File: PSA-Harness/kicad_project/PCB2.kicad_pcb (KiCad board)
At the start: 4 copper layers, 28.3 x 52.5 mm, 15 parts, among them J1 to_EPS_1, J2 to_EPS_2, J3 to_ESP_3, J7 USB_C_Receptacle, J8 B2B_1, J9 B2B_2, U1 DG419LEUA, U2 DG419LEUA

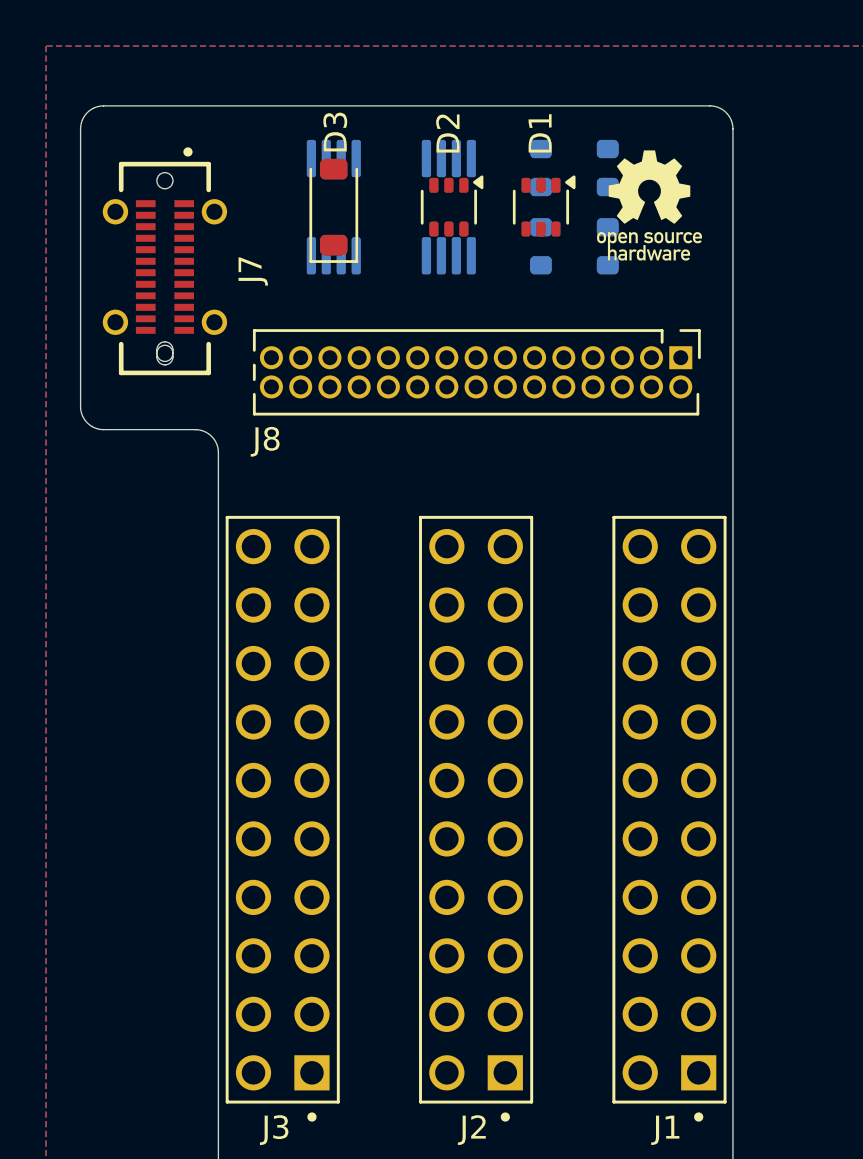
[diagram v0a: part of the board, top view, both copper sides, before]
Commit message: PCB2 CAN routed
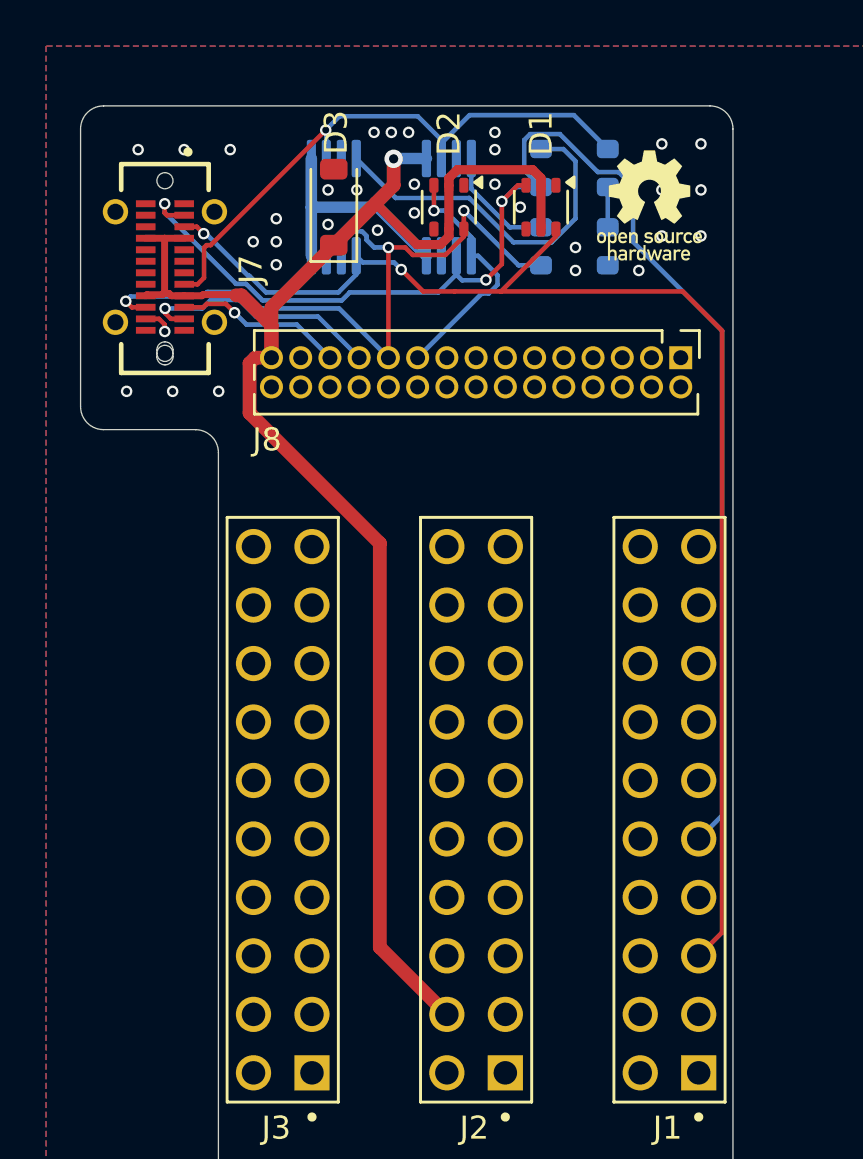
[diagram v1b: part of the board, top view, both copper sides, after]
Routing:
- net +12V: track 0.00 -> 79.9 mm, vias 0 -> 1
- net CAN0_H: track 0.00 -> 64.1 mm, vias 0 -> 3
- net CAN0_L: track 0.00 -> 58.3 mm, vias 0 -> 2
- net CAN2_L: track 0.00 -> 31.1 mm, vias 0 -> 3
- net SBU1: track 0.00 -> 26.5 mm, vias 0 -> 1
- net CAN2_H: track 0.00 -> 25.6 mm, vias 0 -> 2
- net Net-(R2-Pad1): track 0.00 -> 15.7 mm
- net CAN1_H: track 0.00 -> 10.8 mm, vias 0 -> 1
- net CAN1_L: track 0.00 -> 7.36 mm, vias 0 -> 1
- net Net-(R1-Pad2): track 0.00 -> 5.03 mm
- net Net-(R3-Pad2): track 0.00 -> 1.75 mm
- net GND: vias 0 -> 32

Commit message: PCB2 routed
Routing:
- net 1: track 0.00 -> 52.2 mm, vias 0 -> 3
- net 50: track 0.00 -> 50.3 mm, vias 0 -> 2
- net 49: track 0.00 -> 48.8 mm, vias 0 -> 3
- net 54: track 0.00 -> 45.4 mm, vias 0 -> 4
- net 48: track 0.00 -> 43.2 mm, vias 0 -> 1
- net 2: track 0.00 -> 41.3 mm, vias 0 -> 1
- net 28: track 0.00 -> 38.1 mm, vias 0 -> 1
- net 30: track 0.00 -> 38.0 mm, vias 0 -> 1
- net 52: track 0.00 -> 37.6 mm, vias 0 -> 2
- net 47: track 0.00 -> 37.6 mm, vias 0 -> 1
- net 4: track 0.00 -> 36.6 mm, vias 0 -> 3
- net 40: track 0.00 -> 35.7 mm
- net 60: track 0.00 -> 33.4 mm
- net 21: track 0.00 -> 33.3 mm, vias 0 -> 1
- net 29: track 0.00 -> 33.0 mm, vias 0 -> 1
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
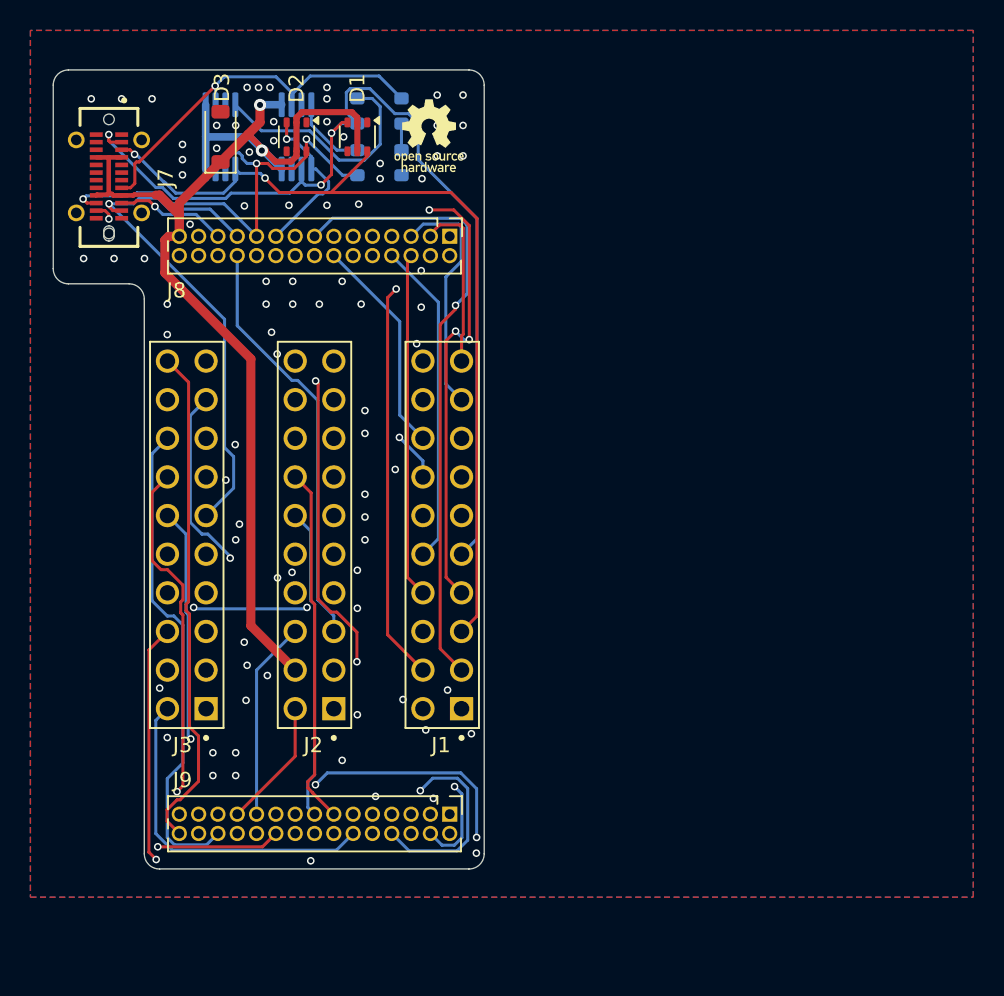
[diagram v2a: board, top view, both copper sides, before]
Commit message: improve PCB2 clearences
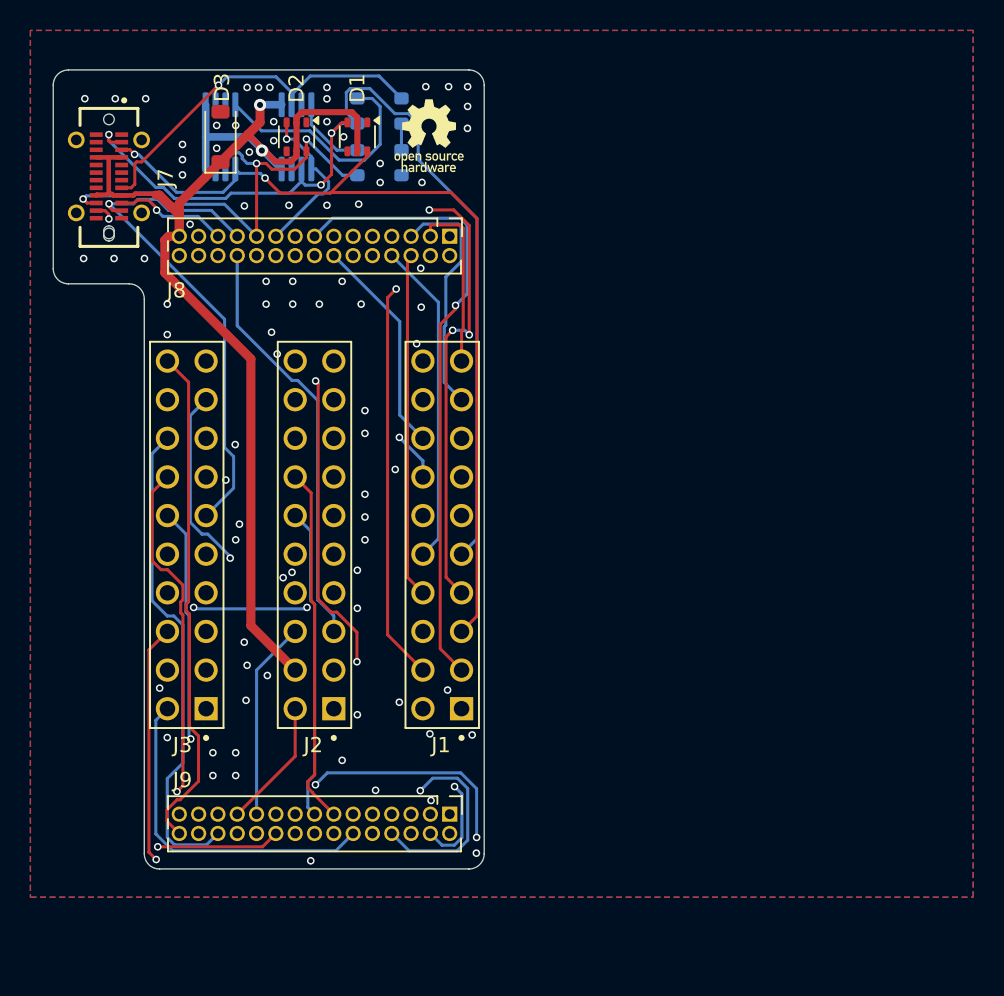
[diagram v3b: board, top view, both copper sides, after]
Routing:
- net GND: vias 68 -> 67
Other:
- rule pad_to_mask_clearance: 0.038 -> 0

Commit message: chg: separate PCB1/2
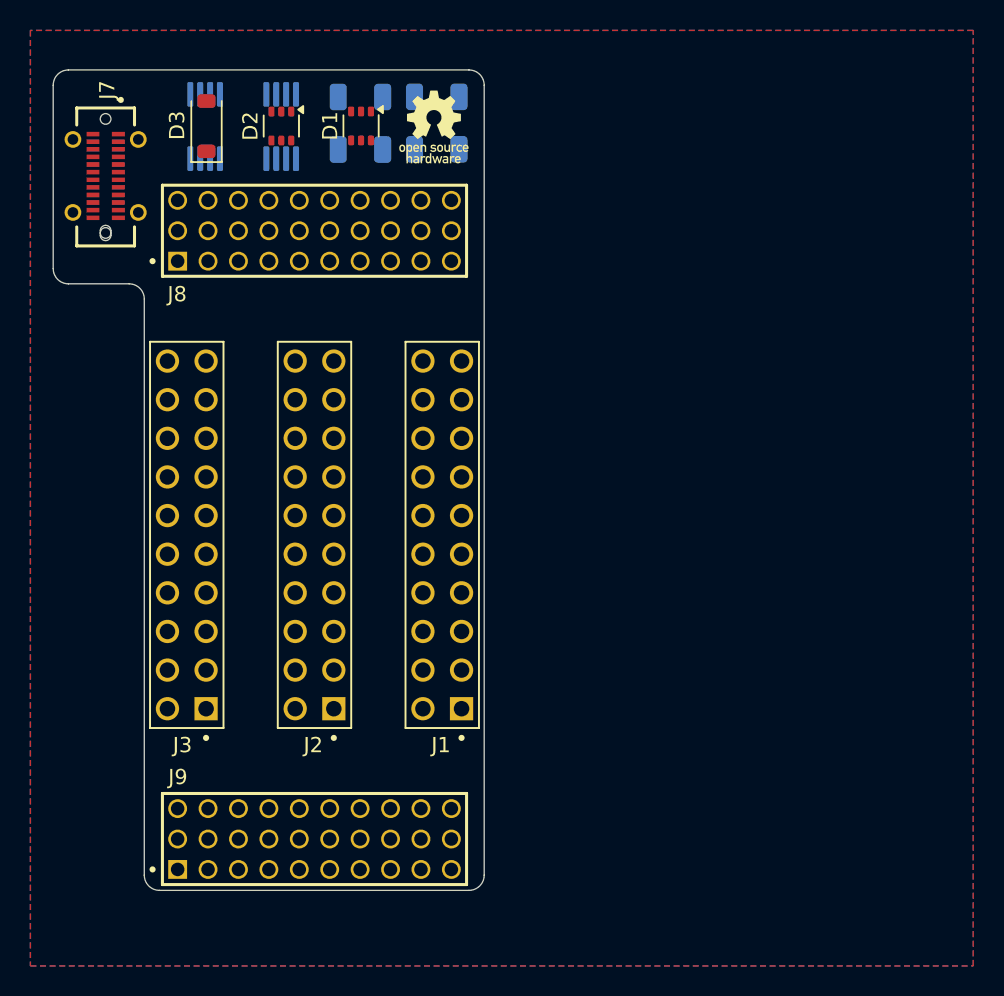
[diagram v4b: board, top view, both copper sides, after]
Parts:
- J8, J9: footprint Connector_PinHeader_1.27mm:PinHeader_2x15_P1.27mm_Vertical -> PSA:SAMTEC_TW-10-X-X-T-X-X
- R1, R2, R3, R4: footprint Resistor_SMD:R_0603_1608Metric -> Resistor_SMD:R_1206_3216Metric
- moved J9 18.3 mm to (96.7, 144.2), turned to 0 degrees
- moved J8 18.0 mm to (96.7, 104.2), turned to 0 degrees
- moved R3 2.50 mm to (113.7, 93.4), turned to 0 degrees
- moved R4 2.48 mm to (113.7, 96.8), turned to 180 degrees
- moved D2 1.23 mm to (103.5, 95.3)
- moved U1 1.22 mm to (98.5, 95.3)
- moved U2 1.22 mm to (103.5, 95.3)
- moved D3 1.16 mm to (98.6, 95.3)
- moved R2 0.94 mm to (108.7, 93.4), turned to 0 degrees
- moved R1 0.89 mm to (108.7, 96.8), turned to 180 degrees
- moved D1 0.76 mm to (108.7, 95.3)
- moved J7 0.22 mm to (91.9, 98.6)
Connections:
- J8 pad 1: 11 -> GND
- J8 pad 11: 6 -> CAN2_H
- J8 pad 13: 4 -> 1
- J8 pad 17: 1 -> 4
- J8 pad 19: CAN2_H -> 6
- J8 pad 21: CAN2_L -> 7
- J8 pad 23: CAN1_H -> 8
- J8 pad 25: CAN1_L -> 9
- J8 pad 27: GND -> 10
- J8 pad 29: +12V -> 11
- J8 pad 3: 10 -> +12V
- J8 pad 5: 9 -> CAN1_L
- J8 pad 7: 8 -> CAN1_H
- J8 pad 9: 7 -> CAN2_L
- J9 pad 1: 43 -> 28
- J9 pad 11: 38 -> 34
- J9 pad 13: 37 -> 35
- J9 pad 17: 35 -> 37
- J9 pad 19: 34 -> 38
- J9 pad 21: 33 -> 39
- J9 pad 23: 31 -> 40
- J9 pad 25: 30 -> 41
- J9 pad 27: 29 -> 42
- J9 pad 29: 28 -> 43
- J9 pad 3: 42 -> 29
- J9 pad 5: 41 -> 30
- J9 pad 7: 40 -> 31
- J9 pad 9: 39 -> 33
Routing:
- net +12V: track 80.2 -> 0.00 mm, vias 2 -> 0
- net CAN0_H: track 64.1 -> 0.00 mm, vias 3 -> 0
- net CAN0_L: track 58.3 -> 0.00 mm, vias 2 -> 0
- net 1: track 52.2 -> 0.00 mm, vias 3 -> 0
- net 50: track 50.3 -> 0.00 mm, vias 2 -> 0
- net 49: track 48.8 -> 0.00 mm, vias 3 -> 0
- net 54: track 45.4 -> 0.00 mm, vias 4 -> 0
- net 48: track 43.5 -> 0.00 mm, vias 1 -> 0
- net 2: track 41.3 -> 0.00 mm, vias 1 -> 0
- net 28: track 38.1 -> 0.00 mm, vias 1 -> 0
- net 30: track 38.0 -> 0.00 mm, vias 1 -> 0
- net 52: track 37.6 -> 0.00 mm, vias 2 -> 0
- net 47: track 37.6 -> 0.00 mm, vias 1 -> 0
- net 4: track 36.3 -> 0.00 mm, vias 3 -> 0
- net 40: track 35.7 -> 0.00 mm
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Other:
- board size 28.3 x 52.5 mm -> 28.3 x 54 mm
- rule pad_to_mask_clearance: 0 -> 0.038

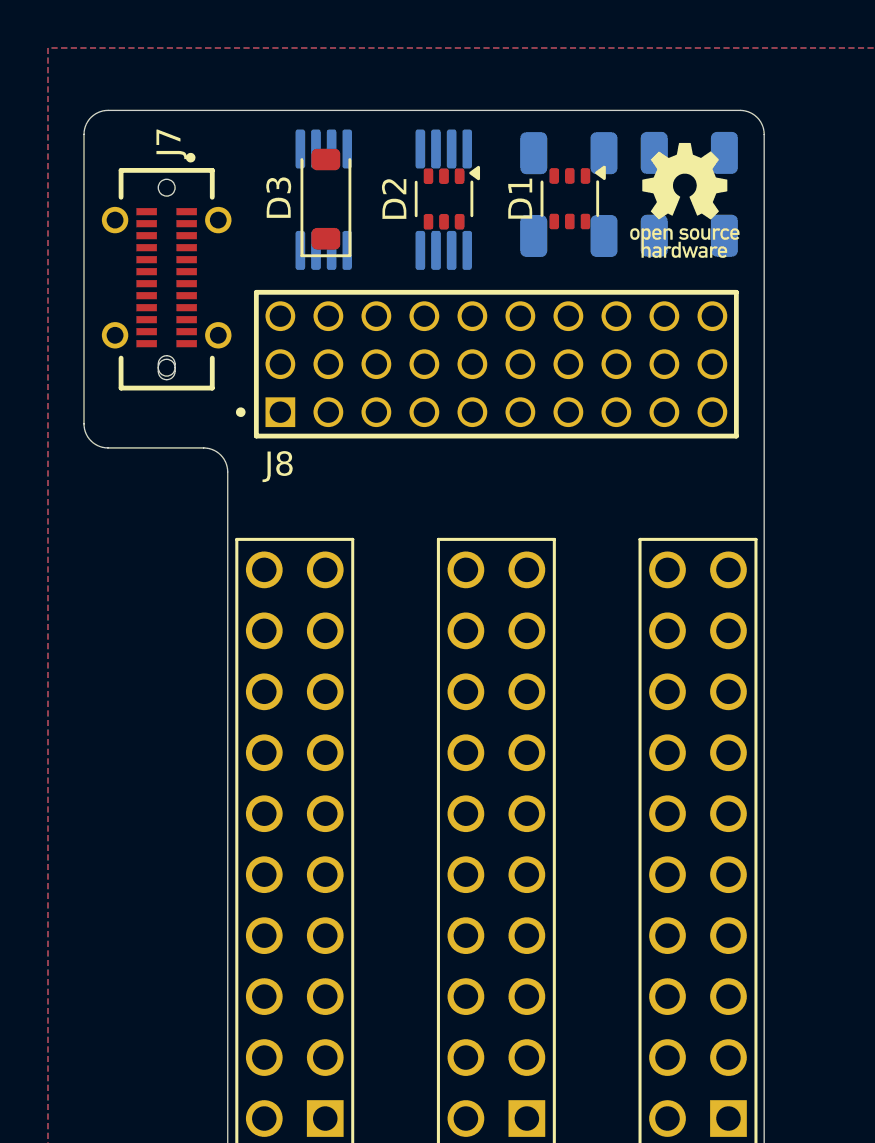
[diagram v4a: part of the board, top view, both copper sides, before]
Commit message: CAN routed
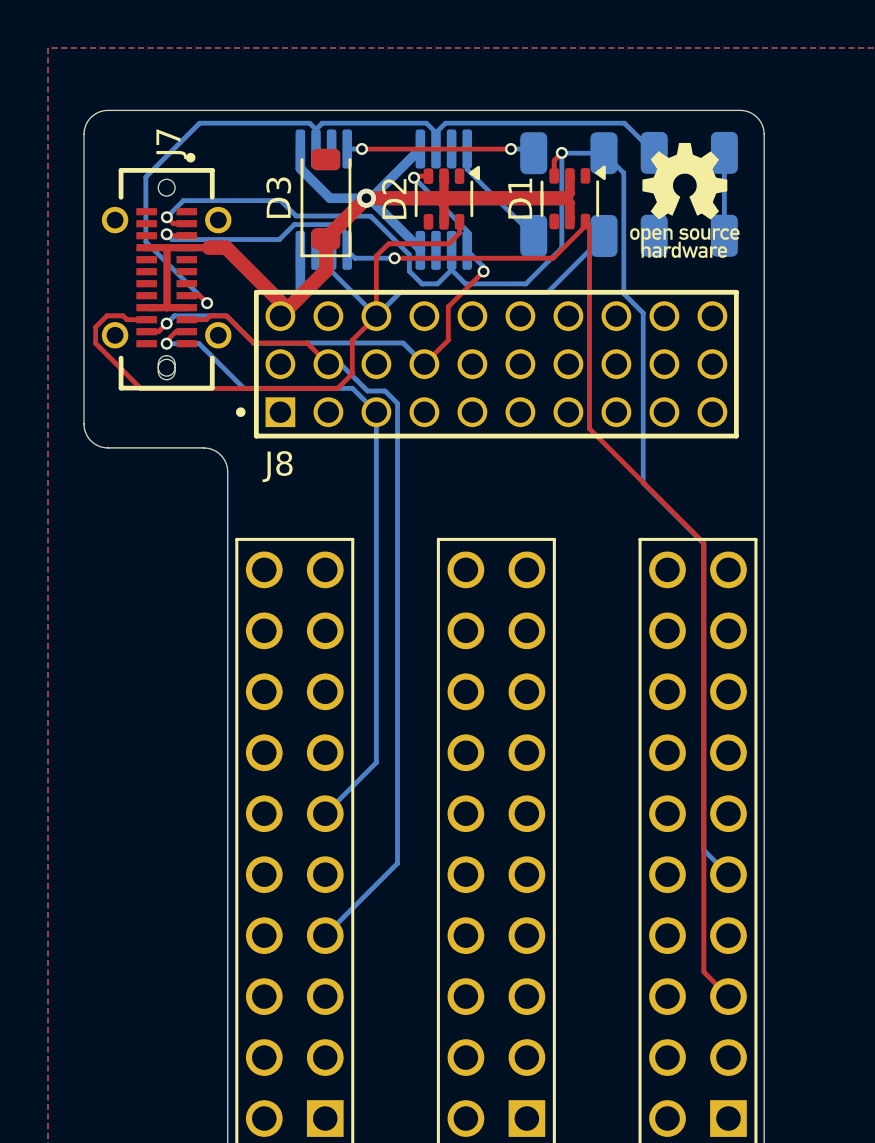
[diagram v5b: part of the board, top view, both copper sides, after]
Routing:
- net CAN0_H: track 0.00 -> 61.3 mm, vias 0 -> 2
- net CAN0_L: track 0.00 -> 55.2 mm, vias 0 -> 2
- net +12V: track 0.00 -> 43.3 mm, vias 0 -> 1
- net CAN2_L: track 0.00 -> 38.8 mm
- net CAN1_L: track 0.00 -> 33.8 mm
- net SBU1: track 0.00 -> 31.9 mm, vias 0 -> 1
- net CAN1_H: track 0.00 -> 28.6 mm, vias 0 -> 1
- net CAN2_H: track 0.00 -> 23.3 mm, vias 0 -> 3
- net Net-(R2-Pad1): track 0.00 -> 7.85 mm, vias 0 -> 2
- net Net-(R1-Pad2): track 0.00 -> 4.77 mm
- net Net-(R3-Pad2): track 0.00 -> 3.45 mm
